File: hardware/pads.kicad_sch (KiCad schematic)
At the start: 27 parts, among them J10 M3, J13 M4, J16 TP0, J17 RP0, J18 5V, J19 GND, J2 +, J20 LED, J21 5V, J22 BZ-, J23 CAM, J24 5V, J25 GND, J26 VHD, J27 GND, J28 TX1, J29 RX1, J3 -, J31 USB, J32 CAM, J33 GND, J4 M1, J7 M2

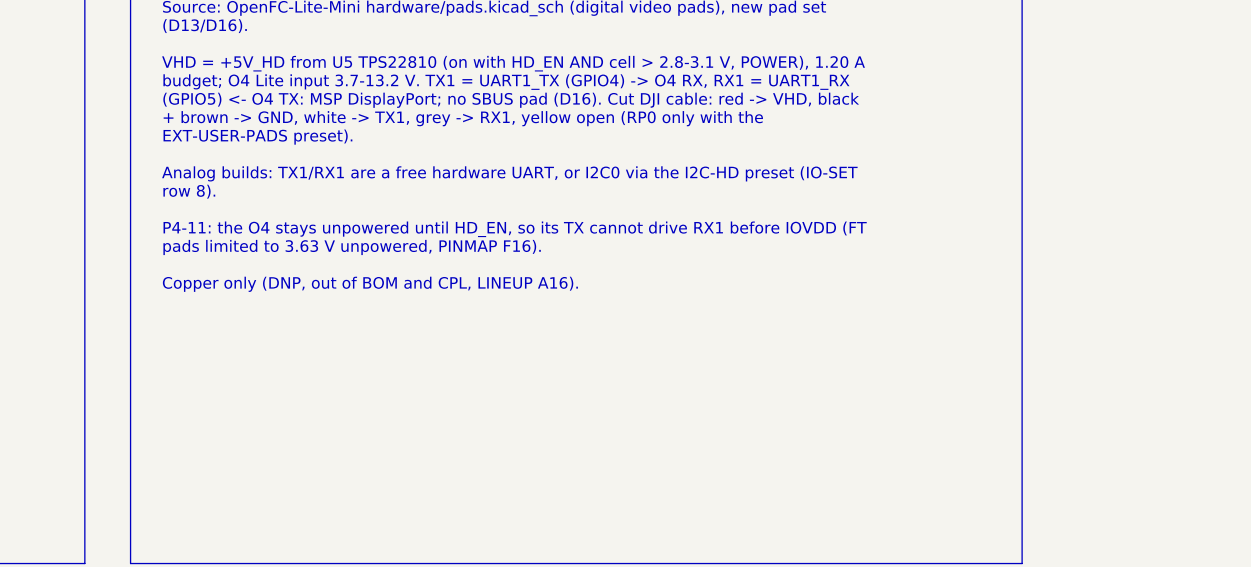
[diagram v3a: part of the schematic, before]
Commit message: hardware: floorplan v3 review pass (RX RF corner blocker fixed; majors listed in FLOORPLAN.md Open)
Co-Authored-By: Claude Opus 5.5 <noreply@anthropic.com>
Claude-Session: https://claude.ai/code/session_01RFaS5jnC9tnPam9GBgmGnG
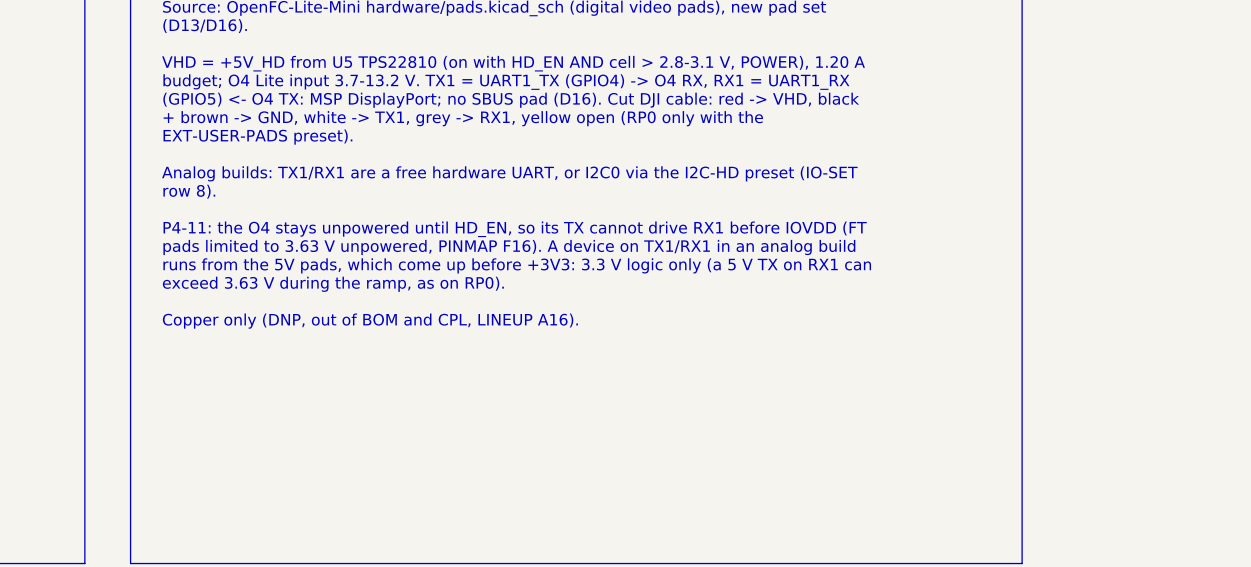
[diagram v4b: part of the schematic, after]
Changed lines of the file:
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@@
 		)
 	)
-	(text_box "Source: OpenFC-Lite-Mini hardware/pads.kicad_sch (digital video pads), new pad set (D13/D16).\n\nVHD = +5V_HD from U5 TPS22810 (on with HD_EN AND cell > 2.8-3.1 V, POWER), 1.20 A budget; O4 Lite input 3.7-13.2 V. TX1 = UART1_TX (GPIO4) -> O4 RX, RX1 = UART1_RX (GPIO5) <- O4 TX: MSP DisplayPort; no SBUS pad (D16). Cut DJI cable: red -> VHD, black + brown -> GND, white -> TX1, grey -> RX1, yellow open (RP0 only with the EXT-USER-PADS preset).\n\nAnalog builds: TX1/RX1 are a free hardware UART, or I2C0 via the I2C-HD preset (IO-SET row 8).\n\nP4-11: the O4 stays unpowered until HD_EN, so its TX cannot drive RX1 before IOVDD (FT pads limited to 3.63 V unpowered, PINMAP F16).\n\nCopper only (DNP, out of BOM and CPL, LINEUP A16)."
+	(text_box "Source: OpenFC-Lite-Mini hardware/pads.kicad_sch (digital video pads), new pad set (D13/D16).\n\nVHD = +5V_HD from U5 TPS22810 (on with HD_EN AND cell > 2.8-3.1 V, POWER), 1.20 A budget; O4 Lite input 3.7-13.2 V. TX1 = UART1_TX (GPIO4) -> O4 RX, RX1 = UART1_RX (GPIO5) <- O4 TX: MSP DisplayPort; no SBUS pad (D16). Cut DJI cable: red -> VHD, black + brown -> GND, white -> TX1, grey -> RX1, yellow open (RP0 only with the EXT-USER-PADS preset).\n\nAnalog builds: TX1/RX1 are a free hardware UART, or I2C0 via the I2C-HD preset (IO-SET row 8).\n\nP4-11: the O4 stays unpowered until HD_EN, so its TX cannot drive RX1 before IOVDD (FT pads limited to 3.63 V unpowered, PINMAP F16). A device on TX1/RX1 in an analog build runs from the 5V pads, which come up before +3V3: 3.3 V logic only (a 5 V TX on RX1 can exceed 3.63 V during the ramp, as on RP0).\n\nCopper only (DNP, out of BOM and CPL, LINEUP A16)."
 		(exclude_from_sim no)
 		(at 309.88 172.72 0)

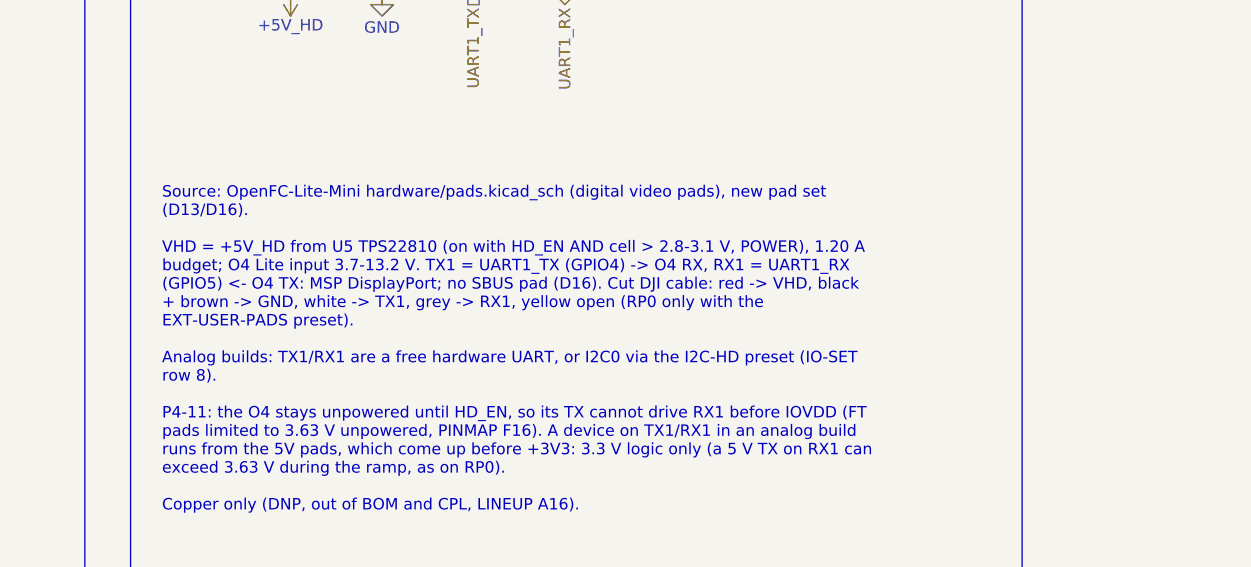
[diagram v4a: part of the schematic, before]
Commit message: wip: routing prep (zones and via fields) and schematic review round 4
Co-Authored-By: Claude Opus 5.5 <noreply@anthropic.com>
Claude-Session: https://claude.ai/code/session_01RFaS5jnC9tnPam9GBgmGnG
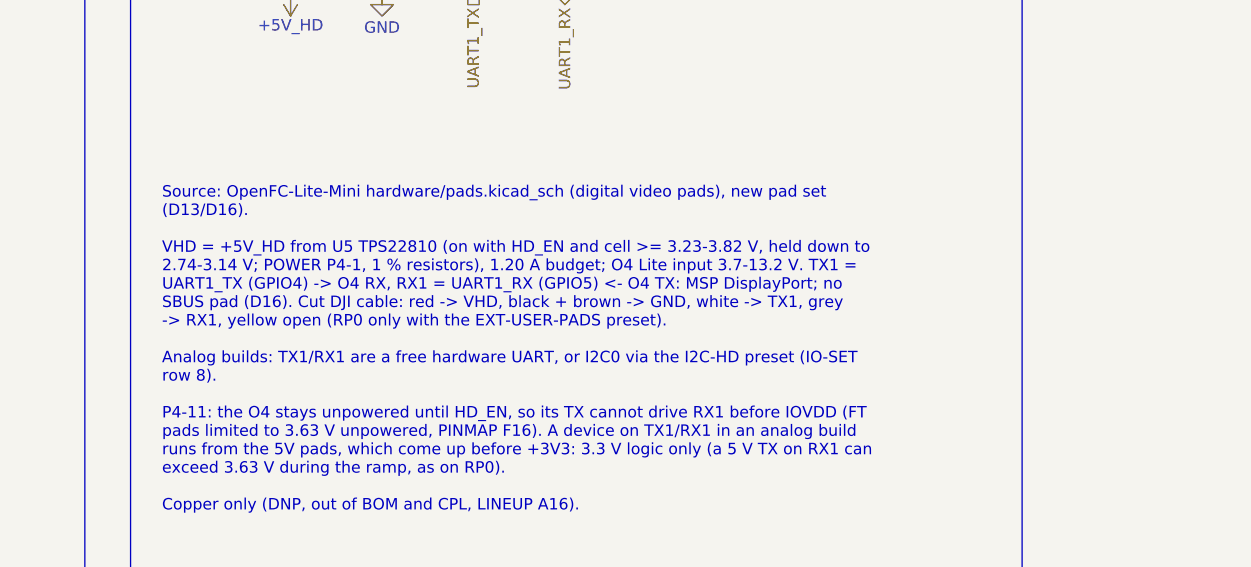
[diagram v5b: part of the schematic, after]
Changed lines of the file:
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@@
 		)
 	)
-	(text_box "Source: OpenFC-Lite-Mini hardware/pads.kicad_sch (digital video pads), new pad set (D13/D16).\n\nVHD = +5V_HD from U5 TPS22810 (on with HD_EN AND cell > 2.8-3.1 V, POWER), 1.20 A budget; O4 Lite input 3.7-13.2 V. TX1 = UART1_TX (GPIO4) -> O4 RX, RX1 = UART1_RX (GPIO5) <- O4 TX: MSP DisplayPort; no SBUS pad (D16). Cut DJI cable: red -> VHD, black + brown -> GND, white -> TX1, grey -> RX1, yellow open (RP0 only with the EXT-USER-PADS preset).\n\nAnalog builds: TX1/RX1 are a free hardware UART, or I2C0 via the I2C-HD preset (IO-SET row 8).\n\nP4-11: the O4 stays unpowered until HD_EN, so its TX cannot drive RX1 before IOVDD (FT pads limited to 3.63 V unpowered, PINMAP F16). A device on TX1/RX1 in an analog build runs from the 5V pads, which come up before +3V3: 3.3 V logic only (a 5 V TX on RX1 can exceed 3.63 V during the ramp, as on RP0).\n\nCopper only (DNP, out of BOM and CPL, LINEUP A16)."
+	(text_box "Source: OpenFC-Lite-Mini hardware/pads.kicad_sch (digital video pads), new pad set (D13/D16).\n\nVHD = +5V_HD from U5 TPS22810 (on with HD_EN and cell >= 3.23-3.82 V, held down to 2.74-3.14 V; POWER P4-1, 1 % resistors), 1.20 A budget; O4 Lite input 3.7-13.2 V. TX1 = UART1_TX (GPIO4) -> O4 RX, RX1 = UART1_RX (GPIO5) <- O4 TX: MSP DisplayPort; no SBUS pad (D16). Cut DJI cable: red -> VHD, black + brown -> GND, white -> TX1, grey -> RX1, yellow open (RP0 only with the EXT-USER-PADS preset).\n\nAnalog builds: TX1/RX1 are a free hardware UART, or I2C0 via the I2C-HD preset (IO-SET row 8).\n\nP4-11: the O4 stays unpowered until HD_EN, so its TX cannot drive RX1 before IOVDD (FT pads limited to 3.63 V unpowered, PINMAP F16). A device on TX1/RX1 in an analog build runs from the 5V pads, which come up before +3V3: 3.3 V logic only (a 5 V TX on RX1 can exceed 3.63 V during the ramp, as on RP0).\n\nCopper only (DNP, out of BOM and CPL, LINEUP A16)."
 		(exclude_from_sim no)
 		(at 309.88 172.72 0)

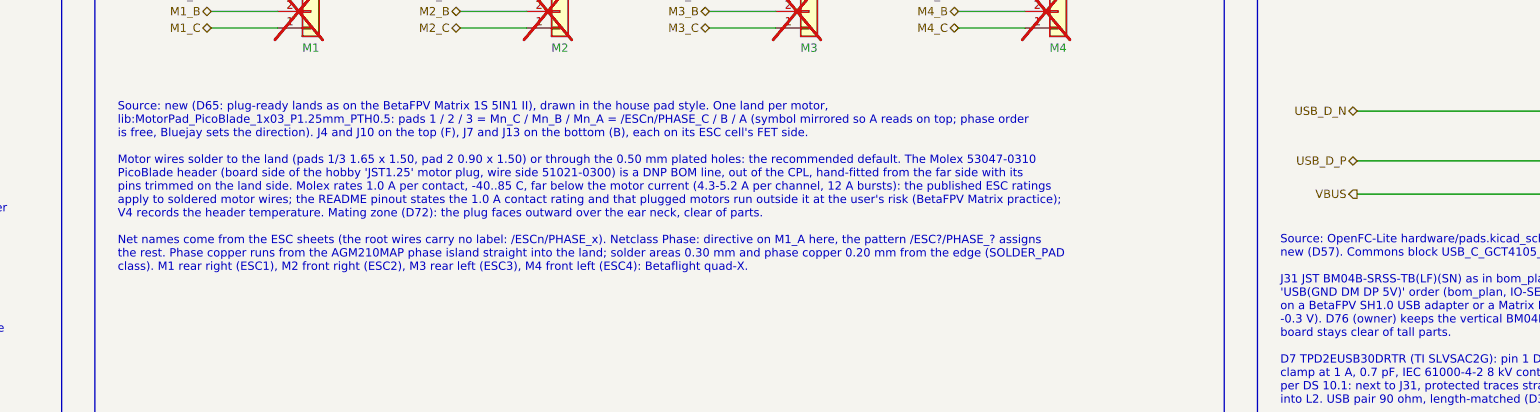
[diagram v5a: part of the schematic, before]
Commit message: schematic: review complete (4 rounds; U20 pin 1 to GND, footprint filters fixed, TPS22810DRVR, R54 270R); ERC 0 errors, check_netlist 7/7; D85-D87
Co-Authored-By: Claude Opus 5.5 <noreply@anthropic.com>
Claude-Session: https://claude.ai/code/session_01RFaS5jnC9tnPam9GBgmGnG
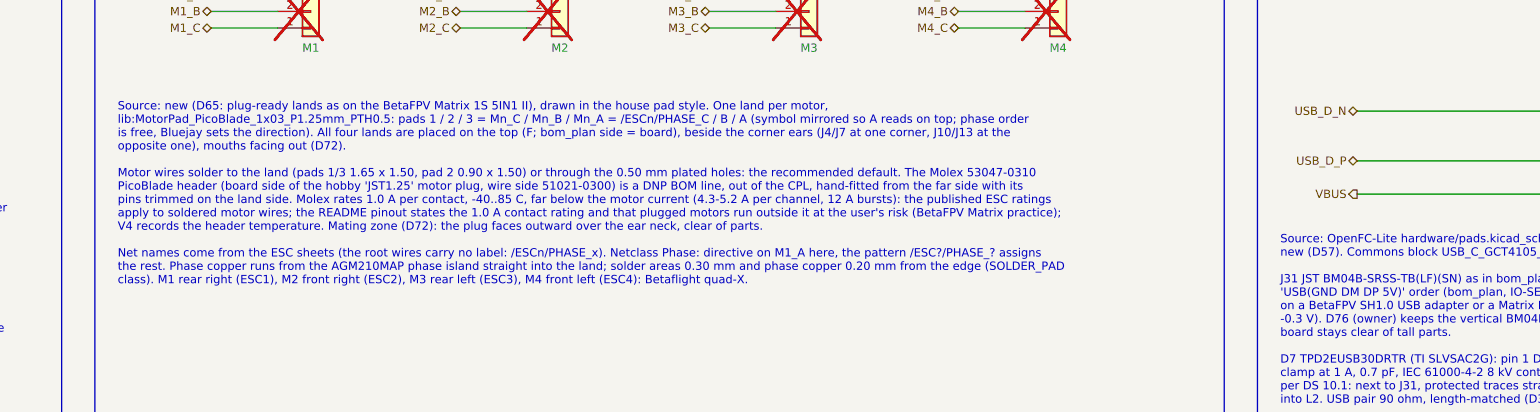
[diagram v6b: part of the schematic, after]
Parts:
- J16, J17, J18, J19, J2, J20, J21, J22, J23, J24, J25, J26, J27, J28, J29, J3, J33: symbol Connector_Generic:Conn_01x01 -> lib:SolderPad_01x01

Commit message: wip: v4 prep in progress (D89 UART pad removal, D93 3D model fixes, Wi-Fi antenna research)
Snapshot of running workflows; final numbers follow when each verifies.

Co-Authored-By: Claude Opus 5.5 <noreply@anthropic.com>
Claude-Session: https://claude.ai/code/session_01RFaS5jnC9tnPam9GBgmGnG
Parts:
- removed J16: TP0, lib:SolderPad_1.0x1.2mm, symbol lib:SolderPad_01x01
- removed J17: RP0, lib:SolderPad_1.0x1.2mm, symbol lib:SolderPad_01x01
- removed J18: 5V, lib:SolderPad_1.0x1.2mm, symbol lib:SolderPad_01x01
- removed J19: GND, lib:SolderPad_1.0x1.2mm, symbol lib:SolderPad_01x01
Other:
- note removed: "User UART pads (PIOUART0)"
- moved on the sheet: J20, J21, J22, J23, J24, J25, J26, J27, J28, J29, J32, J33

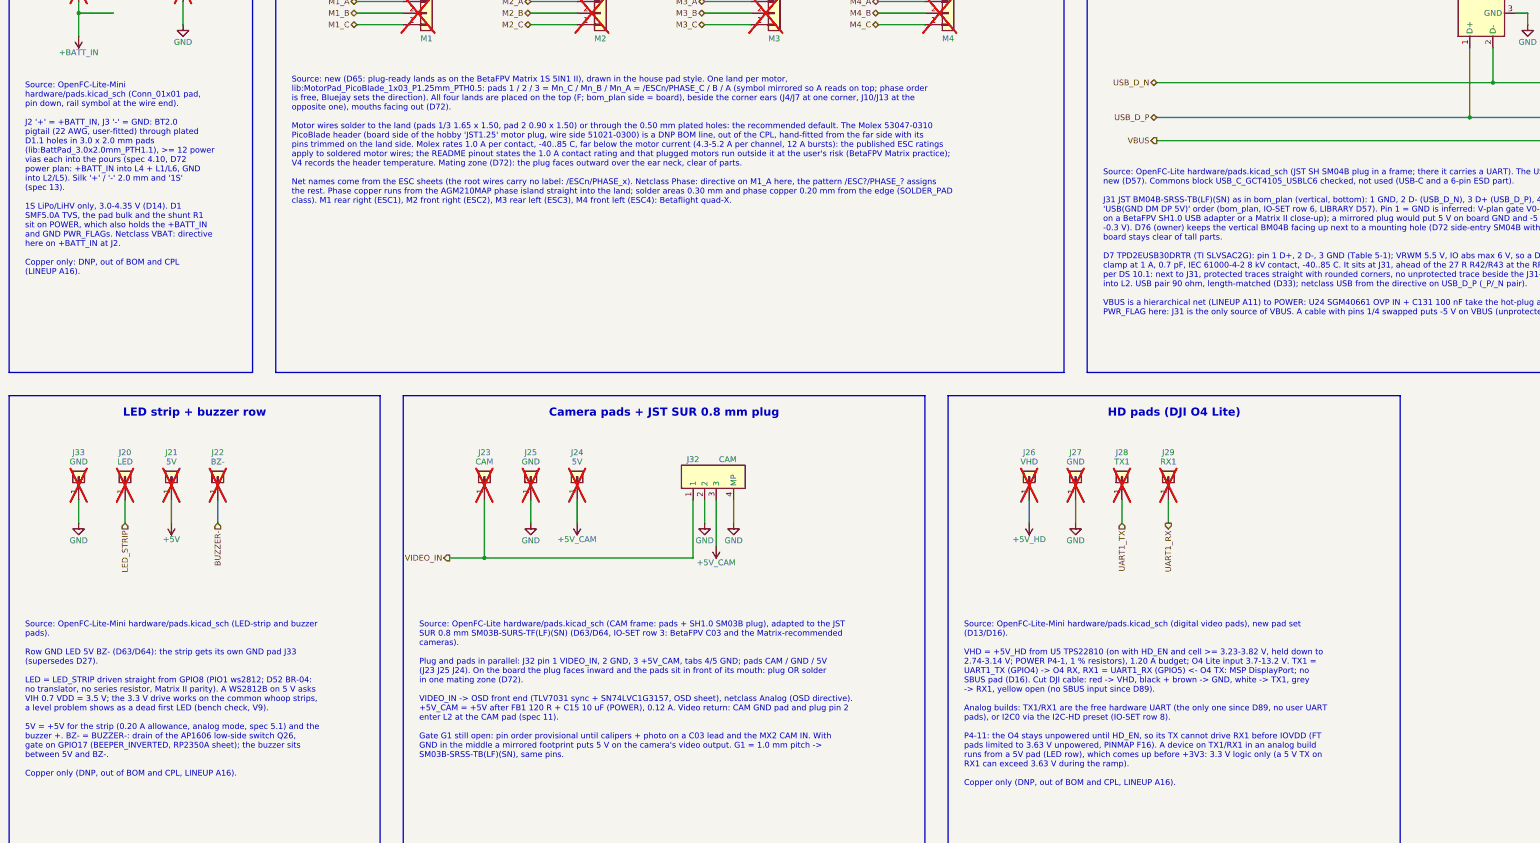
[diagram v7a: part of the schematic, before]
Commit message: WIP final schematic (D111/D113): GPIO map, D100 oscillator, final footprints, lineup power-net names; mid-run snapshot, not yet verified (ERC/netlist/DRU regen pending)
Co-Authored-By: Claude Opus 5.5 <noreply@anthropic.com>
Claude-Session: https://claude.ai/code/session_01RFaS5jnC9tnPam9GBgmGnG
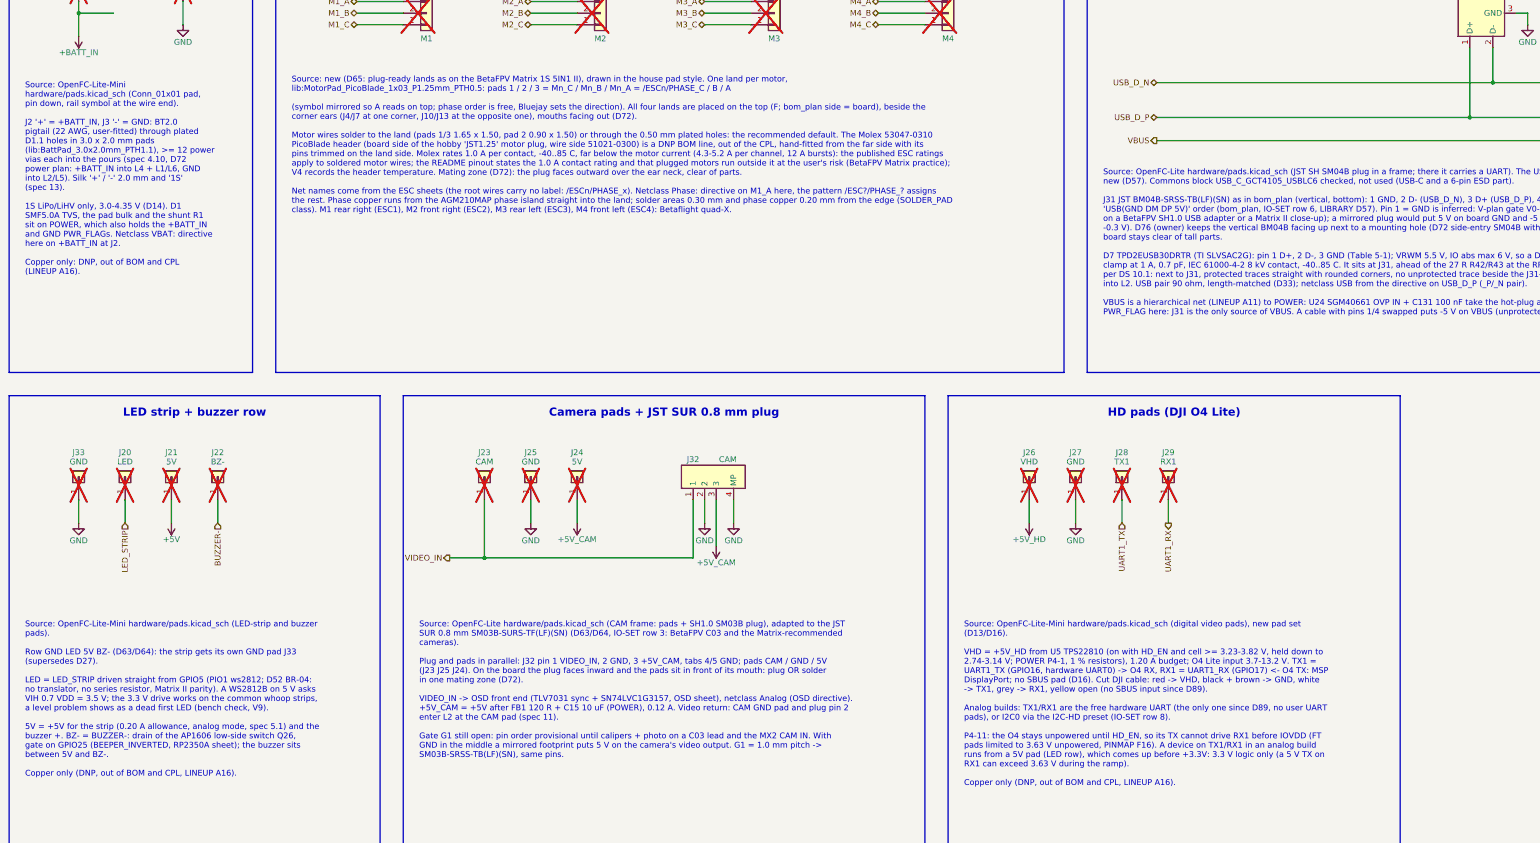
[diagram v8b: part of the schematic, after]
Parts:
- D7: footprint lib:TI_SOT-9X3-3_DRT -> lib:TI_SOT-9X3-3_DRT_L
- J2, J3: footprint lib:BattPad_3.0x2.0mm_PTH1.1 -> lib:BattPad_D1.7mm_PTH1.1
- J20, J21, J22, J33: footprint lib:SolderPad_1.0x1.2mm_Dense -> lib:SolderPad_0.8x1.0mm
- J23, J24, J25, J26, J27, J28, J29: footprint lib:SolderPad_1.0x1.2mm -> lib:SolderPad_0.8x1.0mm
